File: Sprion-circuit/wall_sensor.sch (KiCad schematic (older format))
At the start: 12 parts, among them IC5 NJU6080F1, IC6 NJU6080F1, IC7 NJU6080F1, IC8 NJU6080F1

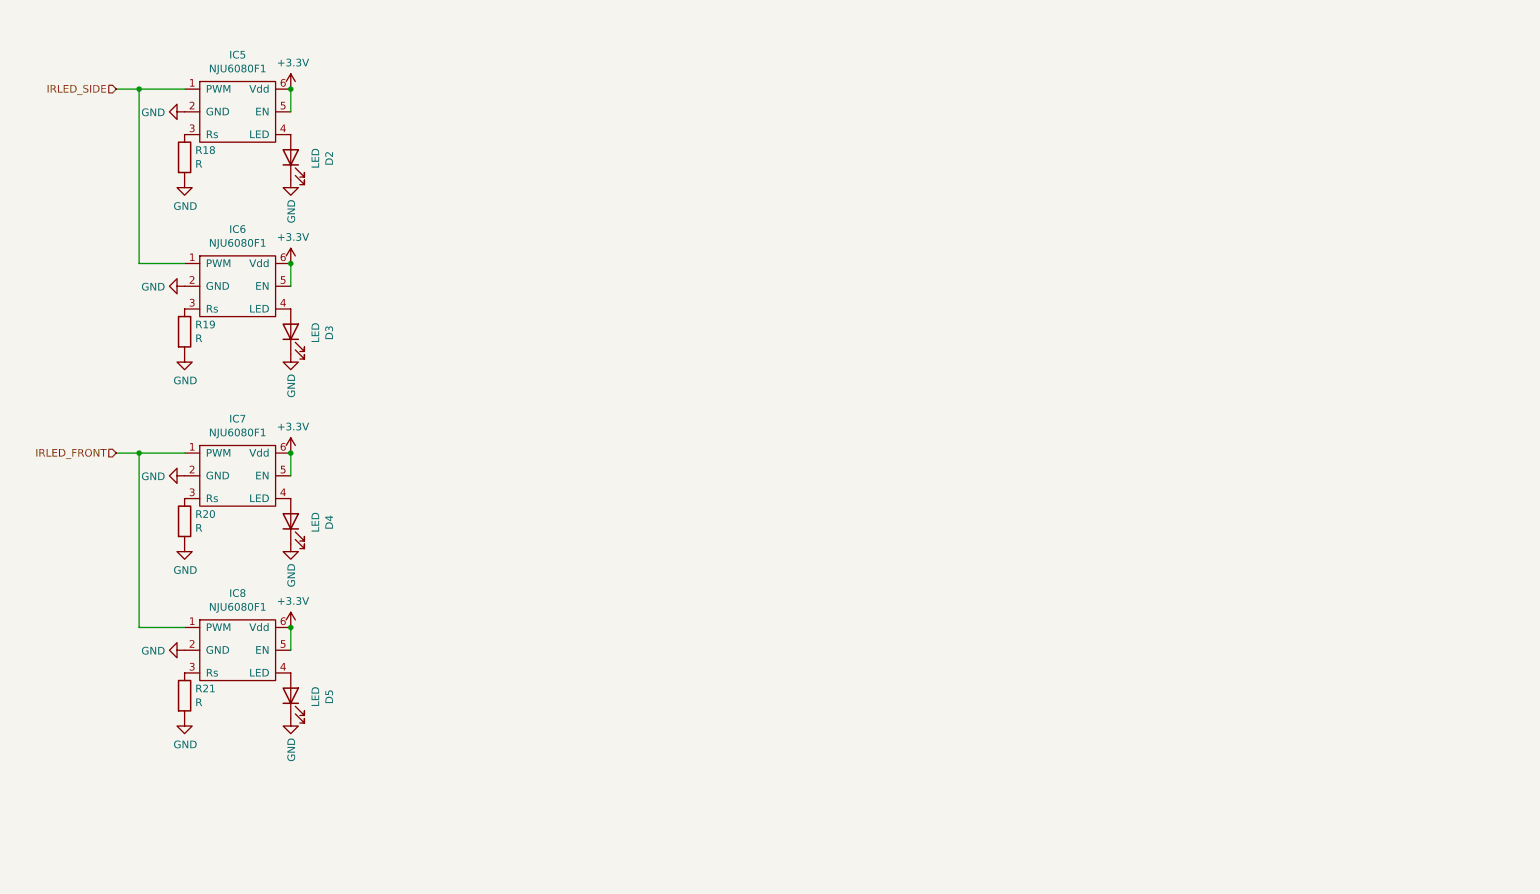
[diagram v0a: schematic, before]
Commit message: add wall sensor
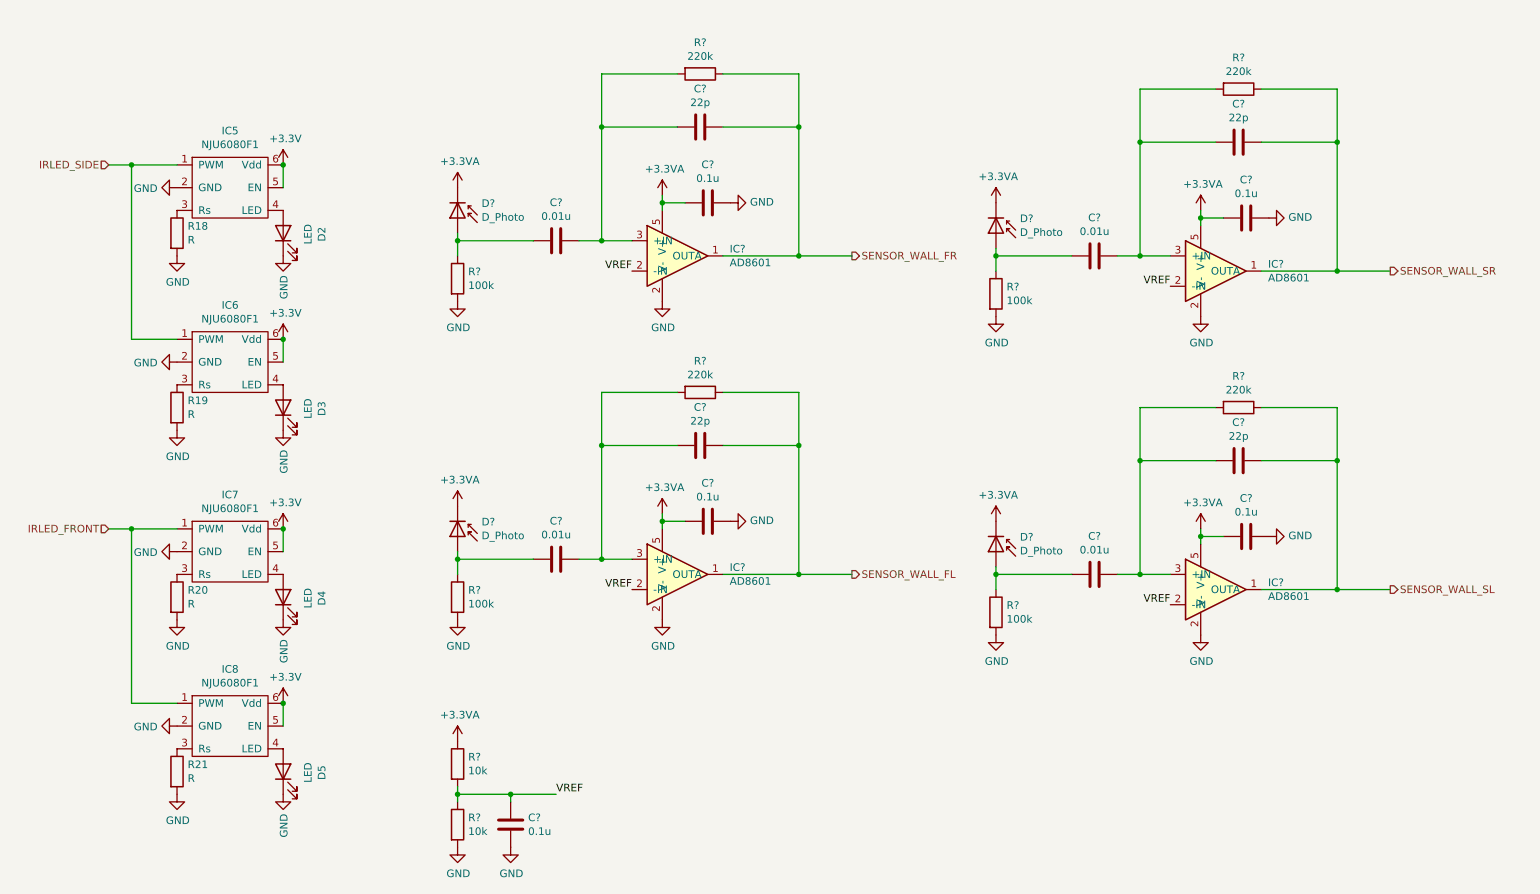
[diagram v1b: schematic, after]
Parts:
- added C? (x4): 0.01u, symbol Device:C
- added C? (x5): 0.1u, symbol Device:C
- added C? (x4): 22p, symbol Device:C
- added D? (x4): D_Photo, symbol Device:D_Photo
- added IC? (x4): AD8601, symbol Sprion-circuit:AD8601
- added R? (x4): 100k, symbol Device:R
- added R? (x2): 10k, symbol Device:R
- added R? (x4): 220k, symbol Device:R
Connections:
- net GND: now also C?.1, C?.1, C?.1, C?.1, C?.2, IC?.2 (V-), IC?.2 (V-), IC?.2 (V-), IC?.2 (V-), R?.2, R?.2, R?.2, R?.2, R?.2
- new net: C?.1, D?.2 (A), R?.1 (x4)
- new net: C?.2, C?.2, IC?.3 (+IN), R?.2 (x4)
- new net +3.3VA: C?.2, C?.2, C?.2, C?.2, D?.1 (K), D?.1 (K), D?.1 (K), D?.1 (K), IC?.5 (V+), IC?.5 (V+), IC?.5 (V+), IC?.5 (V+), R?.1
- new net SENSOR_WALL_FL: C?.1, IC?.1 (OUTA), R?.1
- new net SENSOR_WALL_FR: C?.1, IC?.1 (OUTA), R?.1
- new net SENSOR_WALL_SL: C?.1, IC?.1 (OUTA), R?.1
- new net SENSOR_WALL_SR: C?.1, IC?.1 (OUTA), R?.1
- new net VREF: C?.1, IC?.2 (V-), IC?.2 (V-), IC?.2 (V-), IC?.2 (V-), R?.1, R?.2
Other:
- moved on the sheet: D2, D3, D4, D5, IC5, IC6, IC7, IC8, R18, R19, R20, R21

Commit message: wall sensor
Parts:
- gave numbers to parts that had none: 31
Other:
- moved on the sheet: C15, C16, C17, C18, C19, C20, C21, C22, C23, C24, C25, C26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

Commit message: add,feat,fix:すまんコミットわすれててぐちゃぐちゃや
配置始めた。
フットプリント割り当てた
回路図pdfで吐いた
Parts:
- removed C15: 0.1u, symbol Device:C
- removed IC10, IC11, IC12, IC9: AD8601, symbol Sprion-circuit:AD8601
- removed R24, R25: 10k, symbol Device:R
- added U4, U6, U7, U8: TLV9061, Package_TO_SOT_SMD:SOT-23-6, symbol Sprion-circuit:TLV9061
- C16, C17, C18, C19, C20, C21, C22, C23, C24, C25, C26, C27: footprint (none) -> Capacitor_SMD:C_0603_1608Metric
- D2, D3, D4, D5, D6, D7, D8, D9: footprint (none) -> Connector_PinHeader_2.54mm:PinHeader_1x02_P2.54mm_Vertical
- IC5, IC6, IC7, IC8: footprint (none) -> Package_TO_SOT_SMD:SOT-23-6
- R18, R19, R20, R21, R22, R23, R26, R27, R28, R29, R30, R31: footprint (none) -> Resistor_SMD:R_0603_1608Metric
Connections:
- net +3.3VA: now also U4.5 (SHDN), U4.6 (V+), U6.5 (SHDN), U6.6 (V+), U7.5 (SHDN), U7.6 (V+), U8.5 (SHDN), U8.6 (V+)
- net GND: now also U4.2 (V-), U6.2 (V-), U7.2 (V-), U8.2 (V-)
- net SENSOR_WALL_FL: now also U6.1 (OUTA)
- net SENSOR_WALL_FR: now also U4.1 (OUTA)
- net SENSOR_WALL_SL: now also U8.1 (OUTA)
- net SENSOR_WALL_SR: now also U7.1 (OUTA)
- net VREF: now also U4.4 (-IN), U6.4 (-IN), U7.4 (-IN), U8.4 (-IN)
- net at C16.2, C18.2, R26.2: now also U4.3 (+IN)
- net at C17.2, C19.2, R27.2: now also U6.3 (+IN)
- net at C22.2, C24.2, R30.2: now also U7.3 (+IN)
- net at C23.2, C25.2, R31.2: now also U8.3 (+IN)

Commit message: fix add: 配置 回路の修正
nju6080の出力の修正
配置を完了
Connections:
- net +3V3: now also D2.2 (A), D3.2 (A), D4.2 (A), D5.2 (A)
- net GND: no longer D2.1 (K), D3.1 (K), D4.1 (K), D5.1 (K)
- net at IC5.4 (LED): now also D2.1 (K); no longer D2.2 (A)
- net at IC6.4 (LED): now also D3.1 (K); no longer D3.2 (A)
- net at IC7.4 (LED): now also D4.1 (K); no longer D4.2 (A)
- net at IC8.4 (LED): now also D5.1 (K); no longer D5.2 (A)
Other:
- moved on the sheet: D2, D3, D4, D5
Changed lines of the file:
@@
-$EndComp
-$Comp
-L power:GND #PWR039
-U 1 1 60E5FC48
-P 2750 2400
-F 0 "#PWR039" H 2750 2150 50  0001 C CNN
-F 1 "GND" V 2755 2272 50  0000 R CNN
-F 2 "" H 2750 2400 50  0001 C CNN
-F 3 "" H 2750 2400 50  0001 C CNN
-	1    2750 2400
-	1    0    0    -1
 $EndComp
 $Comp
 L Device:LED D2
 U 1 1 60E5F660
-P 2750 2250
-F 0 "D2" H 2743 1995 50  0000 C CNN
-F 1 "LED" H 2743 2086 50  0000 C CNN
-F 2 "Connector_PinHeader_2.54mm:PinHeader_1x02_P2.54mm_Vertical" H 2750 2250 50  0001 C CNN
-F 3 "~" H 2750 2250 50  0001 C CNN
-	1    2750 2250
+P 3050 1950
+F 0 "D2" H 3043 1695 50  0000 C CNN
+F 1 "LED" H 3043 1786 50  0000 C CNN
+F 2 "Connector_PinHeader_2.54mm:PinHeader_1x02_P2.54mm_Vertical" H 3050 1950 50  0001 C CNN
+F 3 "~" H 3050 1950 50  0001 C CNN
+	1    3050 1950
 	0    -1   -1   0
 $EndComp
@@
 $EndComp
 $Comp
-L power:GND #PWR041
-U 1 1 60E6A72C
-P 2750 3550
-F 0 "#PWR041" H 2750 3300 50  0001 C CNN
-F 1 "GND" V 2755 3422 50  0000 R CNN
-F 2 "" H 2750 3550 50  0001 C CNN
-F 3 "" H 2750 3550 50  0001 C CNN
-	1    2750 3550
-	1    0    0    -1
-$EndComp
-$Comp
 L Device:LED D3
 U 1 1 60E6A732
-P 2750 3400
-F 0 "D3" H 2743 3145 50  0000 C CNN
-F 1 "LED" H 2743 3236 50  0000 C CNN
-F 2 "Connector_PinHeader_2.54mm:PinHeader_1x02_P2.54mm_Vertical" H 2750 3400 50  0001 C CNN
-F 3 "~" H 2750 3400 50  0001 C CNN
-	1    2750 3400
+P 3050 3100
+F 0 "D3" H 3043 2845 50  0000 C CNN
+F 1 "LED" H 3043 2936 50  0000 C CNN
+F 2 "Connector_PinHeader_2.54mm:PinHeader_1x02_P2.54mm_Vertical" H 3050 3100 50  0001 C CNN
+F 3 "~" H 3050 3100 50  0001 C CNN
+	1    3050 3100
 	0    -1   -1   0
 $EndComp
@@
 $EndComp
 $Comp
-L power:GND #PWR043
-U 1 1 60E737E1
-P 2750 4800
-F 0 "#PWR043" H 2750 4550 50  0001 C CNN
-F 1 "GND" V 2755 4672 50  0000 R CNN
-F 2 "" H 2750 4800 50  0001 C CNN
-F 3 "" H 2750 4800 50  0001 C CNN
-	1    2750 4800
-	1    0    0    -1
-$EndComp
-$Comp
 L Device:LED D4
 U 1 1 60E737E7
-P 2750 4650
-F 0 "D4" H 2743 4395 50  0000 C CNN
-F 1 "LED" H 2743 4486 50  0000 C CNN
-F 2 "Connector_PinHeader_2.54mm:PinHeader_1x02_P2.54mm_Vertical" H 2750 4650 50  0001 C CNN
-F 3 "~" H 2750 4650 50  0001 C CNN
-	1    2750 4650
+P 3050 4350
+F 0 "D4" H 3043 4095 50  0000 C CNN
+F 1 "LED" H 3043 4186 50  0000 C CNN
+F 2 "Connector_PinHeader_2.54mm:PinHeader_1x02_P2.54mm_Vertical" H 3050 4350 50  0001 C CNN
+F 3 "~" H 3050 4350 50  0001 C CNN
+	1    3050 4350
 	0    -1   -1   0
 $EndComp
@@
 $EndComp
 $Comp
-L power:GND #PWR045
-U 1 1 60E7380D
-P 2750 5950
-F 0 "#PWR045" H 2750 5700 50  0001 C CNN
-F 1 "GND" V 2755 5822 50  0000 R CNN
-F 2 "" H 2750 5950 50  0001 C CNN
-F 3 "" H 2750 5950 50  0001 C CNN
-	1    2750 5950
-	1    0    0    -1
-$EndComp
-$Comp
 L Device:LED D5
 U 1 1 60E73813
-P 2750 5800
-F 0 "D5" H 2743 5545 50  0000 C CNN
-F 1 "LED" H 2743 5636 50  0000 C CNN
-F 2 "Connector_PinHeader_2.54mm:PinHeader_1x02_P2.54mm_Vertical" H 2750 5800 50  0001 C CNN
-F 3 "~" H 2750 5800 50  0001 C CNN
-	1    2750 5800
+P 3050 5500
+F 0 "D5" H 3043 5245 50  0000 C CNN
+F 1 "LED" H 3043 5336 50  0000 C CNN
+F 2 "Connector_PinHeader_2.54mm:PinHeader_1x02_P2.54mm_Vertical" H 3050 5500 50  0001 C CNN
+F 3 "~" H 3050 5500 50  0001 C CNN
+	1    3050 5500
 	0    -1   -1   0
 $EndComp
@@
 	9000 4300 8800 4300
 Connection ~ 8800 4300
+Wire Wire Line
+	2750 2100 3050 2100
+Wire Wire Line
+	2750 3250 3050 3250
+Wire Wire Line
+	2750 4500 3050 4500
+Wire Wire Line
+	2750 5650 3050 5650
+$Comp
+L power:+3.3V #PWR039
+U 1 1 61BC3282
+P 3050 1800
+F 0 "#PWR039" H 3050 1650 50  0001 C CNN
+F 1 "+3.3V" H 3065 1973 50  0000 C CNN
+F 2 "" H 3050 1800 50  0001 C CNN
+F 3 "" H 3050 1800 50  0001 C CNN
+	1    3050 1800
+	1    0    0    -1
+$EndComp
+$Comp
+L power:+3.3V #PWR041
+U 1 1 61BC4015
+P 3050 2950
+F 0 "#PWR041" H 3050 2800 50  0001 C CNN
+F 1 "+3.3V" H 3065 3123 50  0000 C CNN
+F 2 "" H 3050 2950 50  0001 C CNN
+F 3 "" H 3050 2950 50  0001 C CNN
+	1    3050 2950
+	1    0    0    -1
+$EndComp
+$Comp
+L power:+3.3V #PWR043
+U 1 1 61BC443C
+P 3050 4200
+F 0 "#PWR043" H 3050 4050 50  0001 C CNN
+F 1 "+3.3V" H 3065 4373 50  0000 C CNN
+F 2 "" H 3050 4200 50  0001 C CNN
+F 3 "" H 3050 4200 50  0001 C CNN
+	1    3050 4200
+	1    0    0    -1
+$EndComp
+$Comp
+L power:+3.3V #PWR045
+U 1 1 61BC5117
+P 3050 5350
+F 0 "#PWR045" H 3050 5200 50  0001 C CNN
+F 1 "+3.3V" H 3065 5523 50  0000 C CNN
+F 2 "" H 3050 5350 50  0001 C CNN
+F 3 "" H 3050 5350 50  0001 C CNN
+	1    3050 5350
+	1    0    0    -1
+$EndComp
 $EndSCHEMATC
